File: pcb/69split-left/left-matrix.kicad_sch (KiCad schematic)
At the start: 58 parts, among them SW10 Q, SW11 W, SW12 E, SW13 R, SW14 T, SW15 Caps Lock, SW16 A, SW17 S, SW18 D, SW19 F, SW2 Esc, SW20 G, SW21 Shift, SW22 Z, SW23 X, SW24 C, SW25 V, SW26 B, SW27 Ctrl, SW28 Win, SW29 Alt, SW3 !,1,,F1, SW30 Space, SW4 @,2,,F2, SW5 #,3,,F3, SW6 $,4,,F4, SW7 %,5,,F5, SW8 ^,6,,F6, SW9 Tab

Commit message: Moved things around so it's less confusing.
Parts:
- renumbered D15 to D10, D21 to D11, D27 to D12, D3 to D13, D10 to D14, D16 to D15, D22 to D16, D28 to D17, D4 to D18, D11 to D19, D17 to D20, D23 to D21, D29 to D22, D5 to D23, D12 to D24, D18 to D25, D24 to D26, D6 to D27, D13 to D28, D19 to D29, D1 to D3, D25 to D30, D7 to D31, D8 to D4, D14 to D5, D20 to D6, D26 to D7, D2 to D8, SW22 to SW10, SW28 to SW11, SW4 to SW12, SW11 to SW13, SW17 to SW14, SW23 to SW15, SW29 to SW16, SW5 to SW17, SW12 to SW18, SW18 to SW19, SW24 to SW20, SW30 to SW21, SW6 to SW22, SW13 to SW23, SW19 to SW24, SW7 to SW26, SW14 to SW27, SW20 to SW28, SW26 to SW29, SW9 to SW3, SW8 to SW30, SW15 to SW4, SW21 to SW5, SW27 to SW6, SW3 to SW7, SW10 to SW8, SW16 to SW9

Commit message: Started layout?
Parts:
- SW30: renamed from SW21; footprint Button_Switch_Keyboard:SW_Cherry_MX_2.75u_PCB -> PCM_Switch_Keyboard_Cherry_MX:SW_Cherry_MX_PCB_3.00u
- renumbered D4 to D10, D9 to D11, D14 to D12, D19 to D13, D24 to D14, D28 to D15, D5 to D16, D10 to D17, D15 to D18, D20 to D19, D25 to D20, D29 to D21, D6 to D22, D11 to D23, D16 to D24, D21 to D25, D30 to D27, D7 to D28, D12 to D29, D17 to D30, D22 to D31, D8 to D4, D13 to D5, D18 to D6, D23 to D7, D27 to D8, D31 to D9, SW8 to SW10, SW13 to SW11, SW18 to SW12, SW23 to SW13, SW27 to SW14, SW4 to SW15, SW9 to SW16, SW14 to SW17, SW19 to SW18, SW24 to SW19, SW28 to SW20, SW5 to SW21, SW10 to SW22, SW15 to SW23, SW20 to SW24, SW29 to SW26, SW6 to SW27, SW11 to SW28, SW16 to SW29, SW7 to SW3, SW12 to SW4, SW17 to SW5, SW22 to SW6, SW26 to SW7, SW30 to SW8, SW3 to SW9

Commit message: Continued layout.
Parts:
- D10, D11, D12, D13, D14, D15, D16, D17, D18, D19, D20, D21, D22, D23, D24, D25, D26, D27, D28, D29, D3, D30, D31, D4, D5, D6, D7, D8, D9: footprint Diode_SMD:D_0805_2012Metric_Pad1.15x1.40mm_HandSolder -> Diode_THT:D_DO-35_SOD27_P7.62mm_Horizontal
- SW21: footprint Button_Switch_Keyboard:SW_Cherry_MX_2.25u_PCB -> PCM_Switch_Keyboard_Cherry_MX:SW_Cherry_MX_PCB_2.25u
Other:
- moved on the sheet: D10, D11, D12, D13, D14, D15, D16, D17, D18, D19, D20, D21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

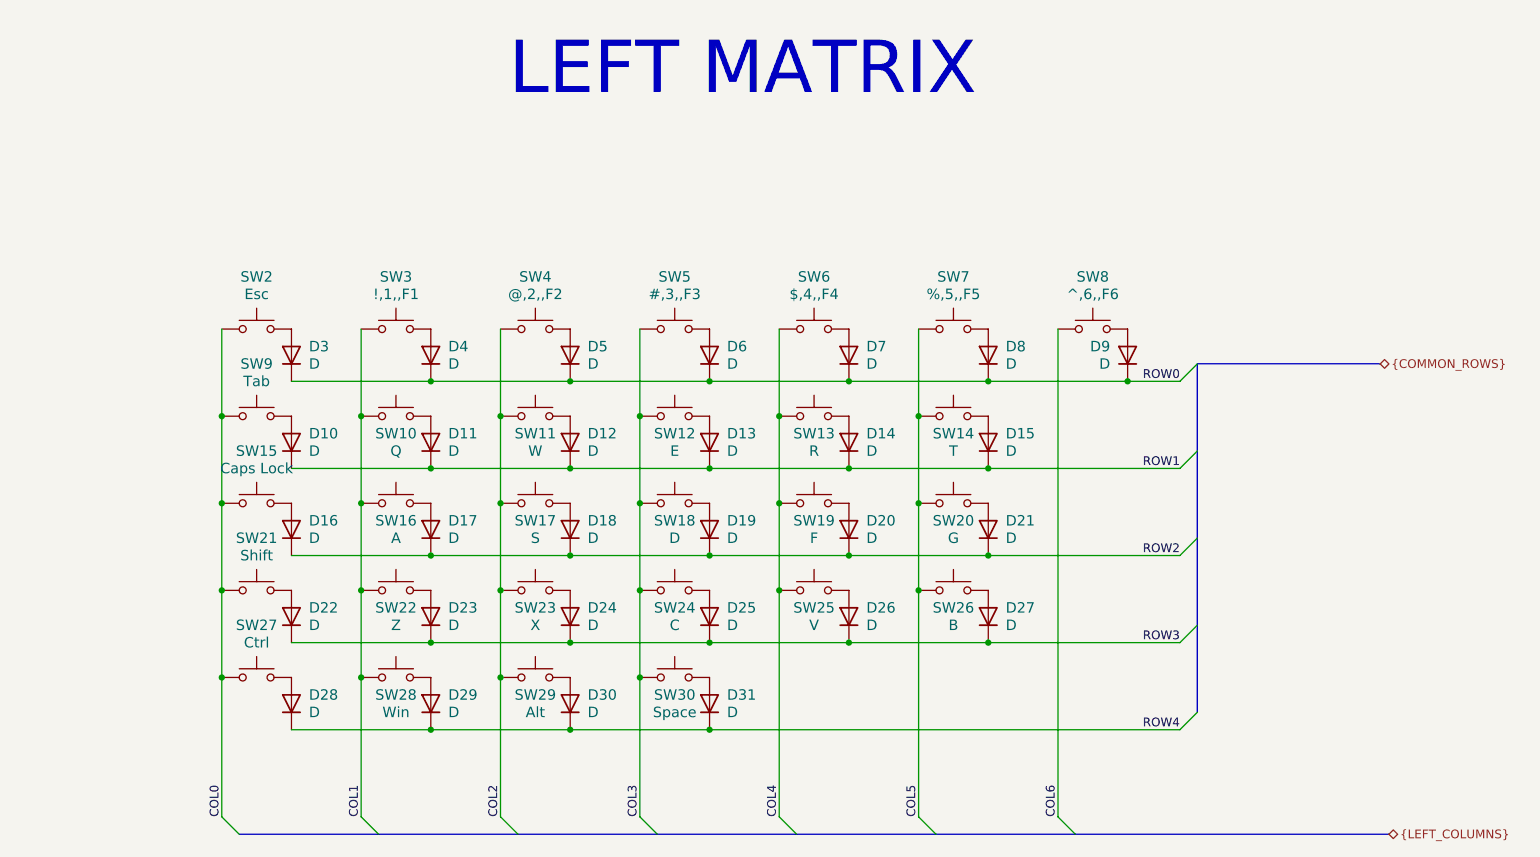
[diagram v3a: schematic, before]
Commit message: Practically finished the left side - need to make a footprint for the split USB connector. Some other schematic changes were made that I will not list. I should've made more commits between ths one and the previous one but it is what it is.
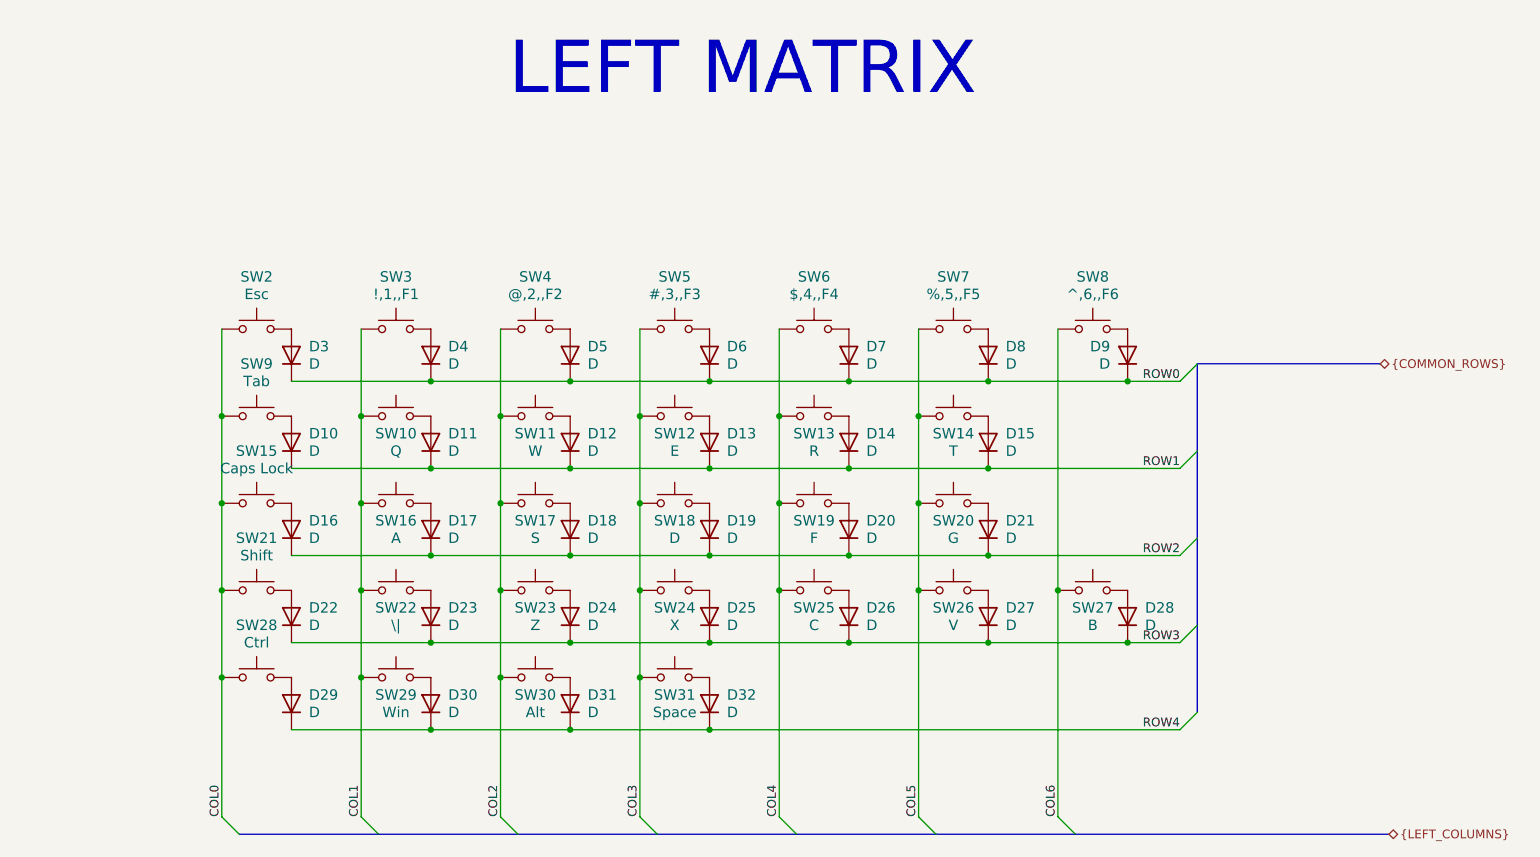
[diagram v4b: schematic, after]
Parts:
- added D23: D, Diode_THT:D_DO-35_SOD27_P7.62mm_Horizontal, symbol Device:D
- added SW22: \|, Button_Switch_Keyboard:SW_Cherry_MX_1.00u_PCB, symbol Switch:SW_Push
- D10, D11, D12, D13, D14, D15, D16, D17, D18, D19, D20, D21, D22, D3, D4, D5, D6, D7, D8, D9: MPN TS4148 RBG -> 1N4454
- D24: renamed from D23; MPN TS4148 RBG -> 1N4454
- D25: renamed from D24; MPN TS4148 RBG -> 1N4454
- D26: renamed from D25; MPN TS4148 RBG -> 1N4454
- D27: renamed from D26; MPN TS4148 RBG -> 1N4454
- D28: renamed from D27; MPN TS4148 RBG -> 1N4454
- D29: renamed from D28; MPN TS4148 RBG -> 1N4454
- D30: renamed from D29; MPN TS4148 RBG -> 1N4454
- D31: renamed from D30; MPN TS4148 RBG -> 1N4454
- D32: renamed from D31; MPN TS4148 RBG -> 1N4454
- SW21: footprint PCM_Switch_Keyboard_Cherry_MX:SW_Cherry_MX_PCB_2.25u -> Button_Switch_Keyboard:SW_Cherry_MX_1.25u_PCB
- SW31: renamed from SW30; footprint PCM_Switch_Keyboard_Cherry_MX:SW_Cherry_MX_PCB_3.00u -> Button_Switch_Keyboard:SW_Cherry_MX_2.75u_PCB
- renumbered SW22 to SW23, SW23 to SW24, SW24 to SW25, SW25 to SW26, SW26 to SW27, SW27 to SW28, SW28 to SW29, SW29 to SW30
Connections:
- net COL1: now also SW22.1; no longer SW23.1
- net COL2: now also SW23.1; no longer SW24.1
- net COL3: now also SW24.1; no longer SW25.1
- net COL4: now also SW25.1; no longer SW26.1
- net COL5: now also SW26.1; no longer SW27.1
- net COL6: now also SW27.1
- net ROW3: now also D23.1 (K)
- new net: D23.2 (A), SW22.2
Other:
- moved on the sheet: D24, D25, D26, D27, D28, SW23, SW24, SW25, SW26, SW27

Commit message: Started changing things gain to use an I/O expander with I2C.
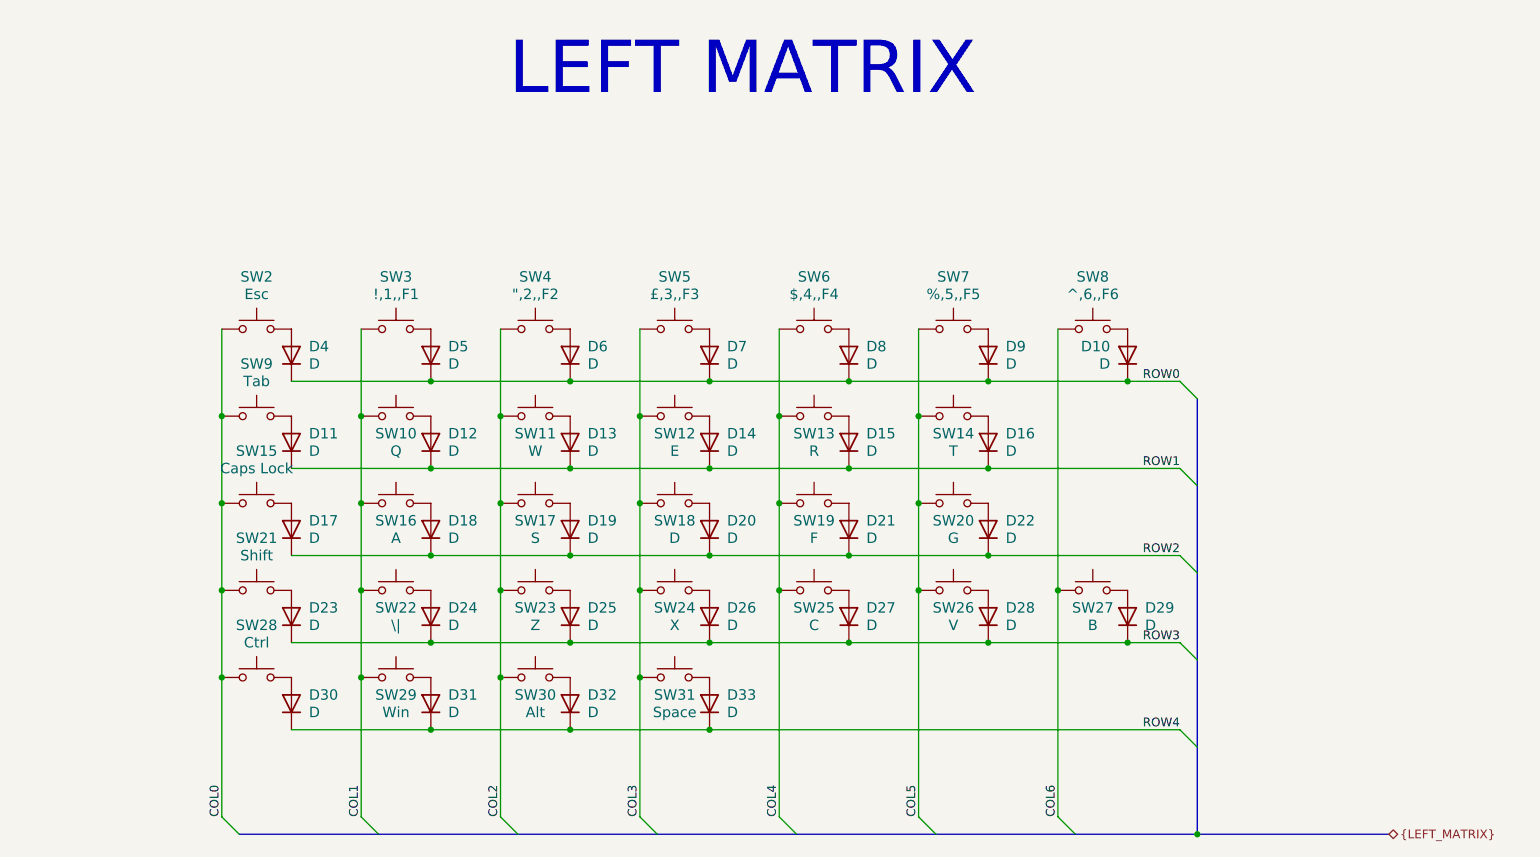
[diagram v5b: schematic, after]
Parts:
- D10: renamed from D9; MPN 1N4454 -> 1N4148
- D11: renamed from D10; MPN 1N4454 -> 1N4148
- D12: renamed from D11; MPN 1N4454 -> 1N4148
- D13: renamed from D12; MPN 1N4454 -> 1N4148
- D14: renamed from D13; MPN 1N4454 -> 1N4148
- D15: renamed from D14; MPN 1N4454 -> 1N4148
- D16: renamed from D15; MPN 1N4454 -> 1N4148
- D17: renamed from D16; MPN 1N4454 -> 1N4148
- D18: renamed from D17; MPN 1N4454 -> 1N4148
- D19: renamed from D18; MPN 1N4454 -> 1N4148
- D20: renamed from D19; MPN 1N4454 -> 1N4148
- D21: renamed from D20; MPN 1N4454 -> 1N4148
- D22: renamed from D21; MPN 1N4454 -> 1N4148
- D23: renamed from D22; MPN 1N4454 -> 1N4148
- D24: renamed from D23; MPN 1N4454 -> 1N4148
- D25: renamed from D24; MPN 1N4454 -> 1N4148
- D26: renamed from D25; MPN 1N4454 -> 1N4148
- D27: renamed from D26; MPN 1N4454 -> 1N4148
- D28: renamed from D27; MPN 1N4454 -> 1N4148
- D29: renamed from D28; MPN 1N4454 -> 1N4148
- D30: renamed from D29; MPN 1N4454 -> 1N4148
- D31: renamed from D30; MPN 1N4454 -> 1N4148
- D32: renamed from D31; MPN 1N4454 -> 1N4148
- D33: renamed from D32; MPN 1N4454 -> 1N4148
- D4: renamed from D3; MPN 1N4454 -> 1N4148
- D5: renamed from D4; MPN 1N4454 -> 1N4148
- D6: renamed from D5; MPN 1N4454 -> 1N4148
- D7: renamed from D6; MPN 1N4454 -> 1N4148
- D8: renamed from D7; MPN 1N4454 -> 1N4148
- D9: renamed from D8; MPN 1N4454 -> 1N4148
- SW4: value @,2,,F2 -> ",2,,F2
- SW5: value #,3,,F3 -> £,3,,F3
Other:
- company: (none) -> Yiannis Michael
- title: 69SPLIT KEYBOARD -> 69SPLIT

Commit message: Minor improvements to left schematic and layout.
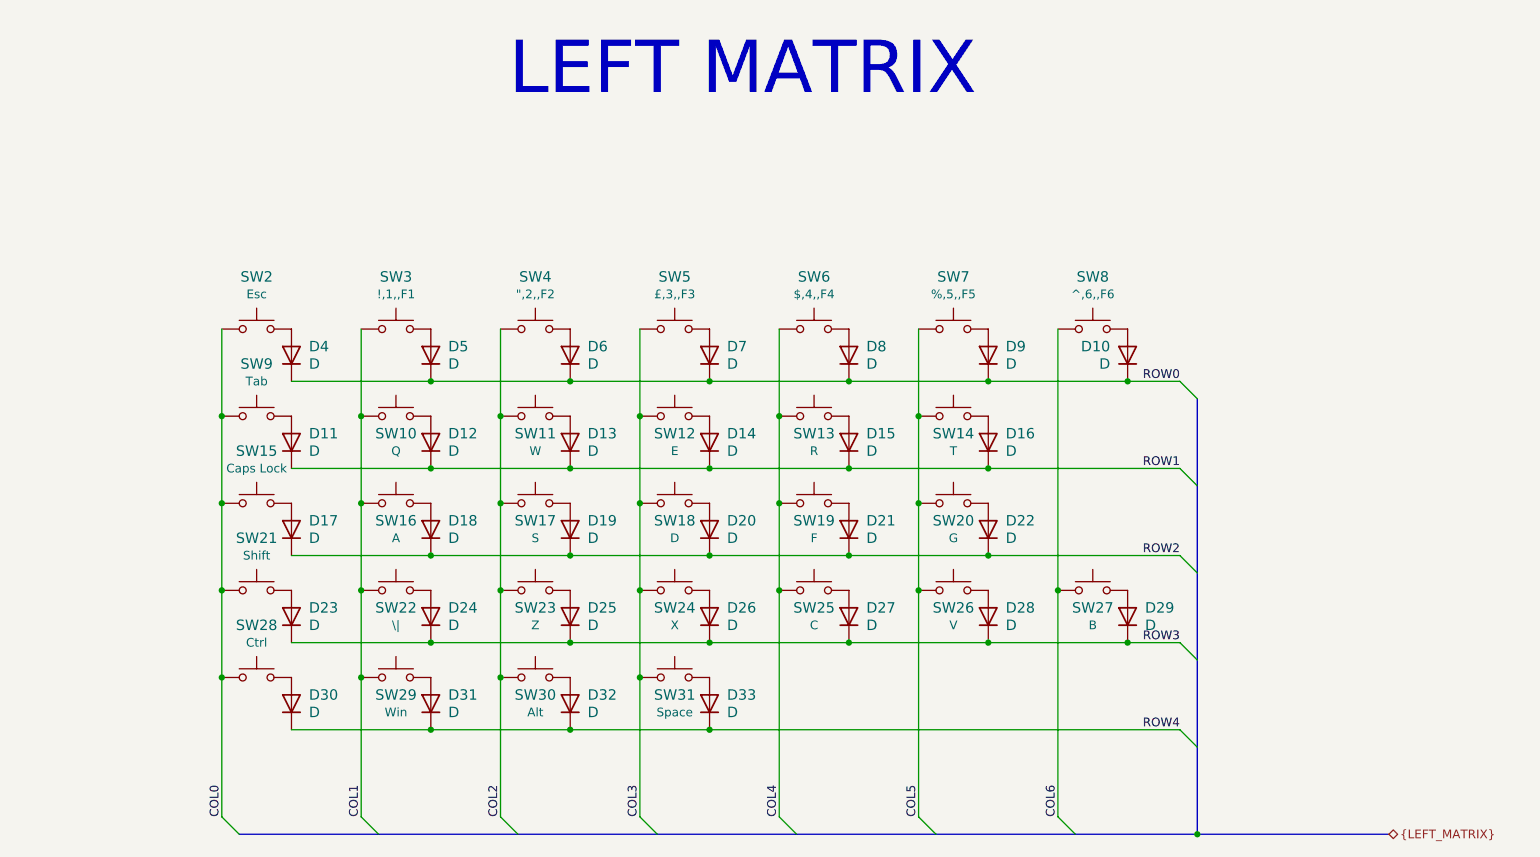
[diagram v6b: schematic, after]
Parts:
- SW10: value Q -> SW_Push; Key (none) -> Q
- SW11: value W -> SW_Push; Key (none) -> W
- SW12: value E -> SW_Push; Key (none) -> E
- SW13: value R -> SW_Push; Key (none) -> R
- SW14: value T -> SW_Push; Key (none) -> T
- SW15: value Caps Lock -> SW_Push; Key (none) -> Caps Lock
- SW16: value A -> SW_Push; Key (none) -> A
- SW17: value S -> SW_Push; Key (none) -> S
- SW18: value D -> SW_Push; Key (none) -> D
- SW19: value F -> SW_Push; Key (none) -> F
- SW2: value Esc -> SW_Push; Key (none) -> Esc
- SW20: value G -> SW_Push; Key (none) -> G
- SW21: value Shift -> SW_Push; Key (none) -> Shift
- SW22: value \| -> SW_Push; Key (none) -> \|
- SW23: value Z -> SW_Push; Key (none) -> Z
- SW24: value X -> SW_Push; Key (none) -> X
- SW25: value C -> SW_Push; Key (none) -> C
- SW26: value V -> SW_Push; Key (none) -> V
- SW27: value B -> SW_Push; Key (none) -> B
- SW28: value Ctrl -> SW_Push; Key (none) -> Ctrl
- SW29: value Win -> SW_Push; Key (none) -> Win
- SW3: value !,1,,F1 -> SW_Push; Key (none) -> !,1,,F1
- SW30: value Alt -> SW_Push; Key (none) -> Alt
- SW31: value Space -> SW_Push; Key (none) -> Space
- SW4: value ",2,,F2 -> SW_Push; Key (none) -> ",2,,F2
- SW5: value £,3,,F3 -> SW_Push; Key (none) -> £,3,,F3
- SW6: value $,4,,F4 -> SW_Push; Key (none) -> $,4,,F4
- SW7: value %,5,,F5 -> SW_Push; Key (none) -> %,5,,F5
- SW8: value ^,6,,F6 -> SW_Push; Key (none) -> ^,6,,F6
- SW9: value Tab -> SW_Push; Key (none) -> Tab
